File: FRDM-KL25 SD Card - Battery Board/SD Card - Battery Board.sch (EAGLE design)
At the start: 59 parts, among them U1 TPS63001, U2 TPS63002, U3 BQ27510DRZT-G3, U4 BQ24210DQCT

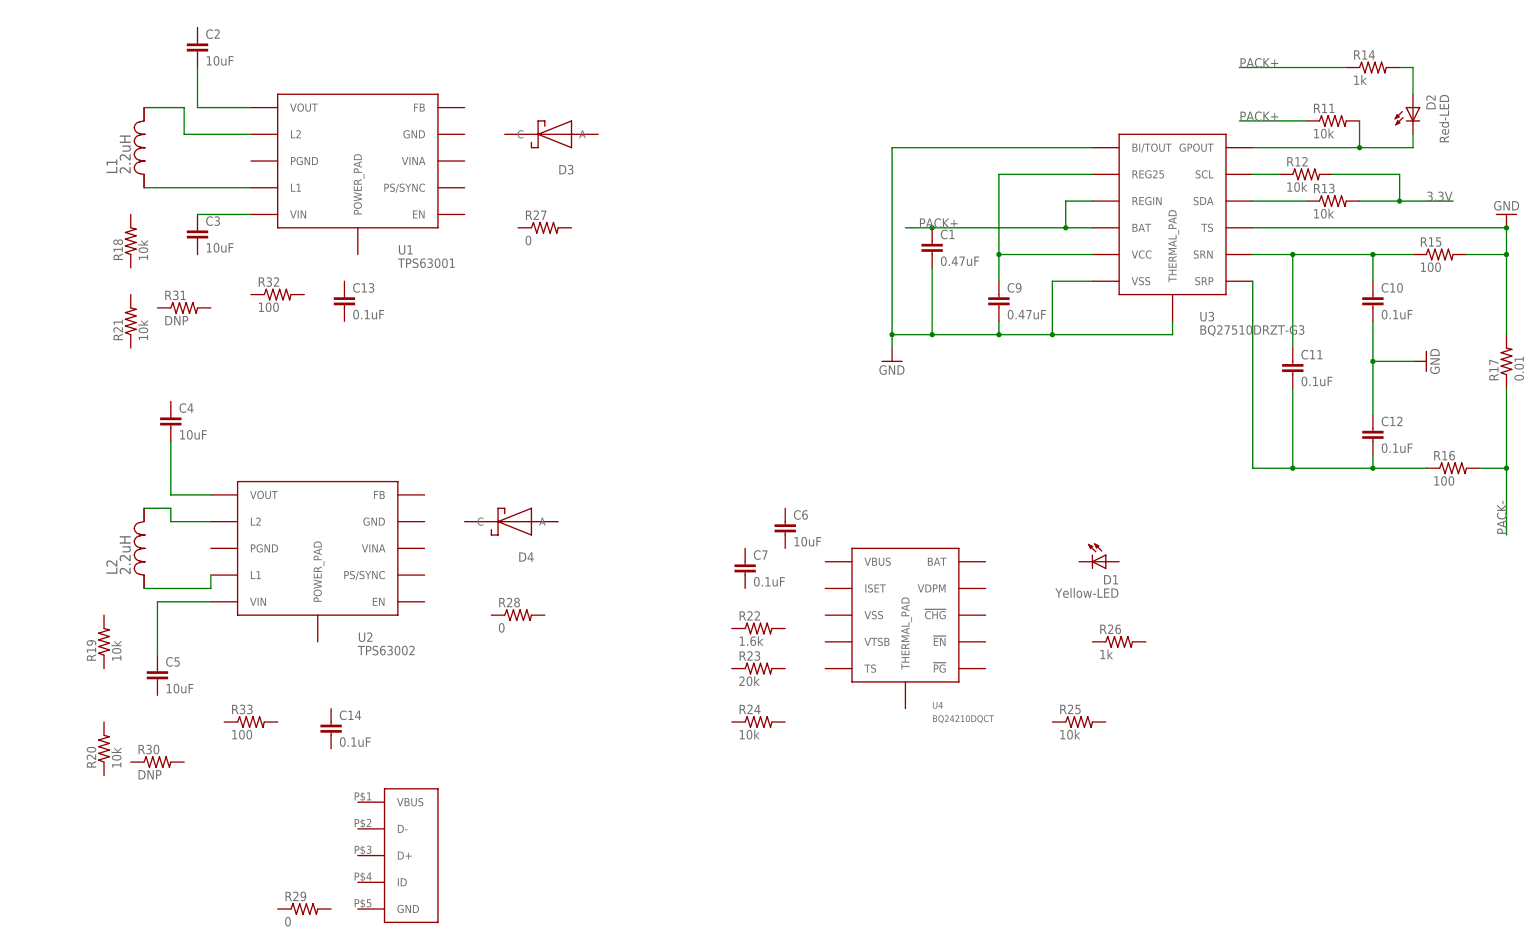
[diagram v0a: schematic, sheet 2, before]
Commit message: FRDM-KL25Z: Connected all components as per the TI Gas Gauge Boosterpack schematic, TPS6300x is connected as per boosterpack but is in disagreement with the datasheet, this will need further investigation to resolve conflicts
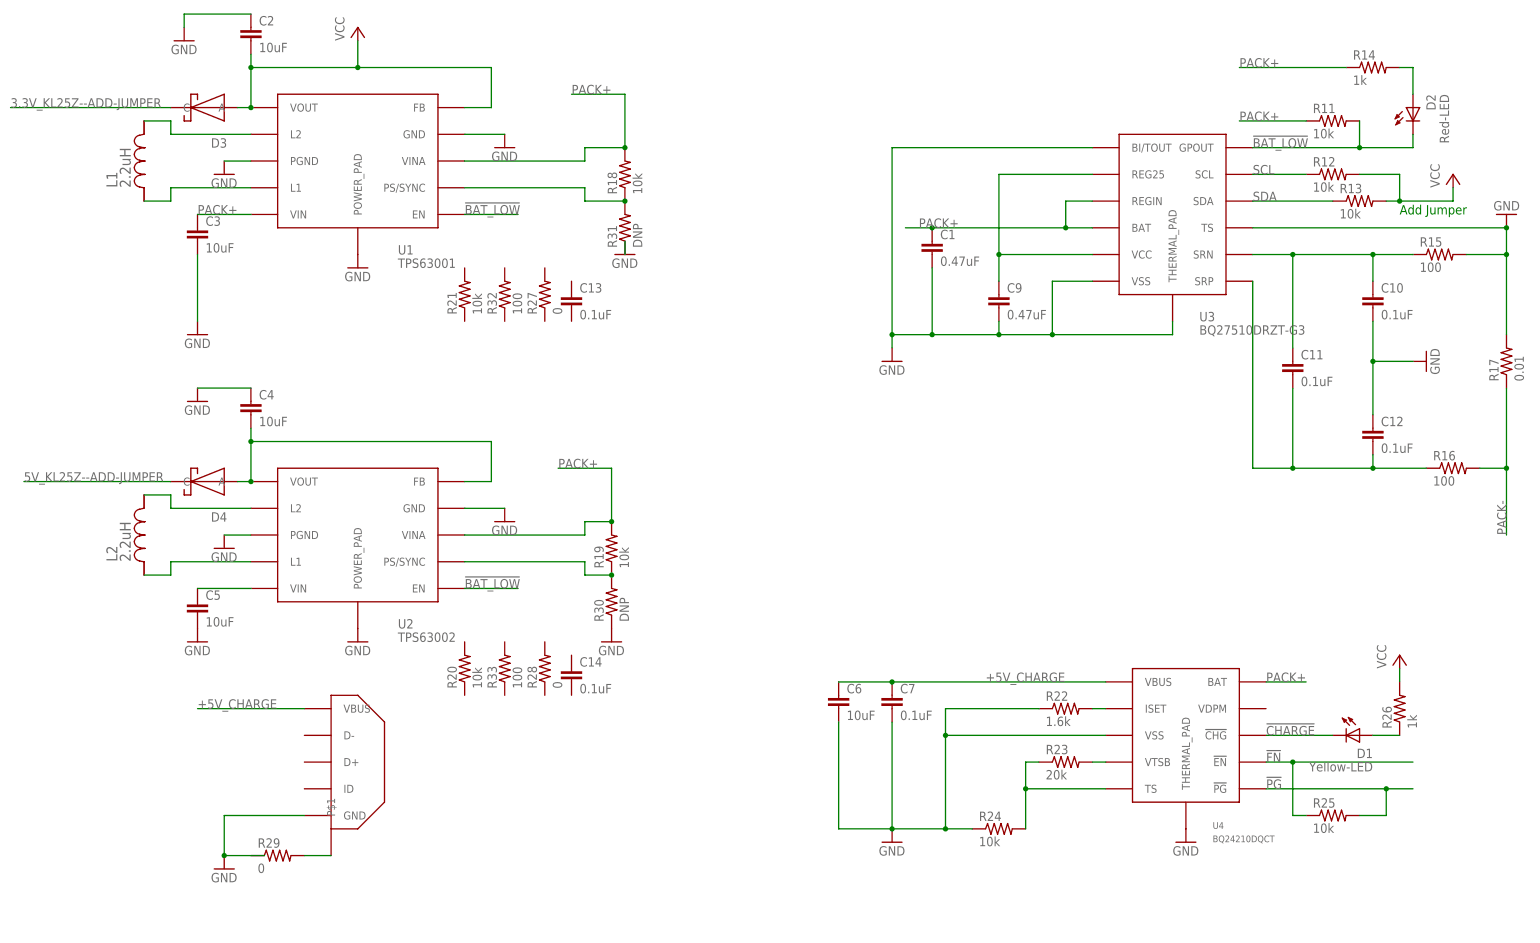
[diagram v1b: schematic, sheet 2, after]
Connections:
- net N$2 renamed SCL
- net N$3 renamed SDA
- removed net 3.3V: R12.2, R13.2
- removed net N$11: C2.2, U1.VOUT
- removed net N$13: C4.2, U2.VOUT
- removed net N$4: D2.C, R11.2, U3.GPOUT
- new net !BAT_LOW: D2.C, R11.2, U1.EN, U2.EN, U3.GPOUT
- new net !CHARGE: D1.C, U4.!CHG
- new net !FN: R25.1, U4.!EN
- new net !PG: R25.2, U4.!PG
- new net +5V_CHARGE: C6.1, C7.1, J2.VBUS, U4.VBUS
- new net 3.3V_KL25Z--ADD-JUMPER: D3.C
- new net 5V_KL25Z--ADD-JUMPER: D4.C
- new net N$2: C4.2, D4.A, U2.FB, U2.VOUT
- new net N$23: R19.1, R30.2, U2.PS/SYNC
- new net N$27: R18.1, R31.2, U1.PS/SYNC
- new net N$28: J2.P$1, R29.2
- new net N$31: R22.2, U4.ISET
- new net N$32: R23.2, U4.VTSB
- new net N$33: R23.1, R24.2, U4.TS
- net GND: now also C2.1, C3.2, C4.1, C5.2, C6.2, C7.2, J2.GND, R22.1, R24.1, R30.1, R31.1, U1.GND, U1.PGND, U1.POWER_PAD, U2.GND, U2.PGND, U2.POWER_PAD, U4.THERMAL_PAD, U4.VSS
- net N$10: now also D1.A, R26.1; no longer C3.1, U1.VIN
- net PACK+: now also C3.1, R18.2, R19.2, U1.VIN, U1.VINA, U2.VINA, U4.BAT
- net VCC: now also C2.2, D3.A, R12.2, R13.2, R26.2, U1.FB, U1.VOUT
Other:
- note added: "Add Jumper"
- note added: "TPS6300x Data Sheet"
- moved on the sheet: C13, C14, C2, C4, C5, C6, C7, D1, D3, D4, L1, L2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

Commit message: FRDM-KL25Z: Aranged components, added board connectors and completed connecting components in teh schematic
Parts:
- added J3, J5: SSW-108-02-S-D, Kas-Connectors:SSW-108-02-S-D
- added J4: SSW-110-02-S-D, Kas-Connectors:SSW-110-02-S-D
- added J6: SSW-106-02-S-D, Kas-Connectors:SSW-106-02-S-D
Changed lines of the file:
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@@
 <part name="P+5" library="Kas-Pwr" deviceset="VCC" device=""/>
 <part name="GND19" library="supply1" deviceset="GND" device=""/>
+<part name="J3" library="Kas-Connectors" deviceset="SSW-108-02-S-D" device=""/>
+<part name="J4" library="Kas-Connectors" deviceset="SSW-110-02-S-D" device=""/>
+<part name="J5" library="Kas-Connectors" deviceset="SSW-108-02-S-D" device=""/>
+<part name="J6" library="Kas-Connectors" deviceset="SSW-106-02-S-D" device=""/>
 </parts>
 <sheets>
@@
 </nets>
 </sheet>
+<sheet>
+<plain>
+</plain>
+<instances>
+<instance part="J3" gate="-1" x="106.68" y="15.24"/>
+<instance part="J3" gate="-2" x="127" y="15.24"/>
+<instance part="J3" gate="-3" x="106.68" y="12.7"/>
+<instance part="J3" gate="-4" x="127" y="12.7"/>
+<instance part="J3" gate="-5" x="106.68" y="10.16"/>
+<instance part="J3" gate="-6" x="127" y="10.16"/>
+<instance part="J3" gate="-7" x="106.68" y="7.62"/>
+<instance part="J3" gate="-8" x="127" y="7.62"/>
+<instance part="J3" gate="-9" x="106.68" y="5.08"/>
+<instance part="J3" gate="-10" x="127" y="5.08"/>
+<instance part="J3" gate="-11" x="106.68" y="2.54"/>
+<instance part="J3" gate="-12" x="127" y="2.54"/>
+<instance part="J3" gate="-13" x="106.68" y="0"/>
+<instance part="J3" gate="-14" x="127" y="0"/>
+<instance part="J3" gate="-15" x="106.68" y="-2.54"/>
+<instance part="J3" gate="-16" x="127" y="-2.54"/>
+<instance part="J4" gate="-1" x="104.14" y="68.58"/>
+<instance part="J4" gate="-2" x="124.46" y="68.58"/>
+<instance part="J4" gate="-3" x="104.14" y="66.04"/>
+<instance part="J4" gate="-4" x="124.46" y="66.04"/>
+<instance part="J4" gate="-5" x="104.14" y="63.5"/>
+<instance part="J4" gate="-6" x="124.46" y="63.5"/>
+<instance part="J4" gate="-7" x="104.14" y="60.96"/>
+<instance part="J4" gate="-8" x="124.46" y="60.96"/>
+<instance part="J4" gate="-9" x="104.14" y="58.42"/>
+<instance part="J4" gate="-10" x="124.46" y="58.42"/>
+<instance part="J4" gate="-11" x="104.14" y="55.88"/>
+<instance part="J4" gate="-12" x="124.46" y="55.88"/>
+<instance part="J4" gate="-13" x="104.14" y="53.34"/>
+<instance part="J4" gate="-14" x="124.46" y="53.34"/>
+<instance part="J4" gate="-15" x="104.14" y="50.8"/>
+<instance part="J4" gate="-16" x="124.46" y="50.8"/>
+<instance part="J4" gate="-17" x="104.14" y="48.26"/>
+<instance part="J4" gate="-18" x="124.46" y="48.26"/>
+<instance part="J4" gate="-19" x="104.14" y="45.72"/>
+<instance part="J4" gate="-20" x="124.46" y="45.72"/>
+<instance part="J5" gate="-1" x="30.48" y="66.04"/>
+<instance part="J5" gate="-2" x="50.8" y="66.04"/>
+<instance part="J5" gate="-3" x="30.48" y="63.5"/>
+<instance part="J5" gate="-4" x="50.8" y="63.5"/>
+<instance part="J5" gate="-5" x="30.48" y="60.96"/>
+<instance part="J5" gate="-6" x="50.8" y="60.96"/>
+<instance part="J5" gate="-7" x="30.48" y="58.42"/>
+<instance part="J5" gate="-8" x="50.8" y="58.42"/>
+<instance part="J5" gate="-9" x="30.48" y="55.88"/>
+<instance part="J5" gate="-10" x="50.8" y="55.88"/>
+<instance part="J5" gate="-11" x="30.48" y="53.34"/>
+<instance part="J5" gate="-12" x="50.8" y="53.34"/>
+<instance part="J5" gate="-13" x="30.48" y="50.8"/>
+<instance part="J5" gate="-14" x="50.8" y="50.8"/>
+<instance part="J5" gate="-15" x="30.48" y="48.26"/>
+<instance part="J5" gate="-16" x="50.8" y="48.26"/>
+<instance part="J6" gate="-1" x="38.1" y="20.32"/>
+<instance part="J6" gate="-2" x="58.42" y="20.32"/>
+<instance part="J6" gate="-3" x="38.1" y="17.78"/>
+<instance part="J6" gate="-4" x="58.42" y="17.78"/>
+<instance part="J6" gate="-5" x="38.1" y="15.24"/>
+<instance part="J6" gate="-6" x="58.42" y="15.24"/>
+<instance part="J6" gate="-7" x="38.1" y="12.7"/>
+<instance part="J6" gate="-8" x="58.42" y="12.7"/>
+<instance part="J6" gate="-9" x="38.1" y="10.16"/>
+<instance part="J6" gate="-10" x="58.42" y="10.16"/>
+<instance part="J6" gate="-11" x="38.1" y="7.62"/>
+<instance part="J6" gate="-12" x="58.42" y="7.62"/>
+</instances>
+<busses>
+</busses>
+<nets>
+</nets>
+</sheet>

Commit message: FRDM-KL25Z: Changed 10k resistors on page to from 0603 to 0402 and added missing files
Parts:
- R11, R12, R13, R18, R19, R20, R21, R24, R25: device Kas-Resistors:RESISTOR10K-100M-0.5%-75V -> Kas-Resistors:RESISTOR10K-62.5M-1%-50V
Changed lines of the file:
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@@
 <part name="U4" library="Kas-Buck Boost Battery Control" deviceset="B224210" device="" value="BQ24210DQCT"/>
 <part name="GND1" library="supply1" deviceset="GND" device=""/>
-<part name="R11" library="Kas-Resistors" deviceset="RESISTOR" device="10K-100M-0.5%-75V" value="10k"/>
-<part name="R12" library="Kas-Resistors" deviceset="RESISTOR" device="10K-100M-0.5%-75V" value="10k"/>
-<part name="R13" library="Kas-Resistors" deviceset="RESISTOR" device="10K-100M-0.5%-75V" value="10k"/>
+<part name="R11" library="Kas-Resistors" deviceset="RESISTOR" device="10K-62.5M-1%-50V" value="10k"/>
+<part name="R12" library="Kas-Resistors" deviceset="RESISTOR" device="10K-62.5M-1%-50V" value="10k"/>
+<part name="R13" library="Kas-Resistors" deviceset="RESISTOR" device="10K-62.5M-1%-50V" value="10k"/>
 <part name="D2" library="Kas-Diodes-LEDs" deviceset="1.6X3.2" device="R-1.85V-20MA" value="Red-LED"/>
 <part name="R14" library="Kas-Resistors" deviceset="RESISTOR" device="1K-62.5M-0.1%-75V" value="1k"/>
@@
 <part name="R16" library="Kas-Resistors" deviceset="RESISTOR" device="100-62.5M-0.1%-75V" value="100"/>
 <part name="R17" library="Kas-Resistors" deviceset="RESISTOR" device="0.01-100M-1%-50V" value="0.01"/>
-<part name="R18" library="Kas-Resistors" deviceset="RESISTOR" device="10K-100M-0.5%-75V" value="10k"/>
-<part name="R19" library="Kas-Resistors" deviceset="RESISTOR" device="10K-100M-0.5%-75V" value="10k"/>
-<part name="R20" library="Kas-Resistors" deviceset="RESISTOR" device="10K-100M-0.5%-75V" value="10k"/>
-<part name="R21" library="Kas-Resistors" deviceset="RESISTOR" device="10K-100M-0.5%-75V" value="10k"/>
+<part name="R18" library="Kas-Resistors" deviceset="RESISTOR" device="10K-62.5M-1%-50V" value="10k"/>
+<part name="R19" library="Kas-Resistors" deviceset="RESISTOR" device="10K-62.5M-1%-50V" value="10k"/>
+<part name="R20" library="Kas-Resistors" deviceset="RESISTOR" device="10K-62.5M-1%-50V" value="10k"/>
+<part name="R21" library="Kas-Resistors" deviceset="RESISTOR" device="10K-62.5M-1%-50V" value="10k"/>
 <part name="R22" library="Kas-Resistors" deviceset="RESISTOR" device="1.6K-125M-0.1%-100V" value="1.6k"/>
 <part name="R23" library="Kas-Resistors" deviceset="RESISTOR" device="20K-63M-1%-50V" value="20k"/>
-<part name="R24" library="Kas-Resistors" deviceset="RESISTOR" device="10K-100M-0.5%-75V" value="10k"/>
-<part name="R25" library="Kas-Resistors" deviceset="RESISTOR" device="10K-100M-0.5%-75V" value="10k"/>
+<part name="R24" library="Kas-Resistors" deviceset="RESISTOR" device="10K-62.5M-1%-50V" value="10k"/>
+<part name="R25" library="Kas-Resistors" deviceset="RESISTOR" device="10K-62.5M-1%-50V" value="10k"/>
 <part name="R26" library="Kas-Resistors" deviceset="RESISTOR" device="1K-62.5M-0.1%-75V" value="1k"/>
 <part name="D1" library="Kas-Diodes-LEDs" deviceset="1.6X3.2" device="Y-X.XX-XXMA" value="Yellow-LED"/>
